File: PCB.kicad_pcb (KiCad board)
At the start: 4 copper layers, 33 parts, among them J2 JST - 1.00mm 4 Pin, SW1 MX_SW_solder, SW2 MX_SW_solder, SW3 MX_SW_solder, SW4 MX_SW_solder, SW72 SW_Push, SW73 SW_Push, U1 RP2040, U2 MX25R3235FZNxx0, U3 USBLC6-2SC6, U4 AP2127N3-1.2, Y1 Crystal_GND24_Small

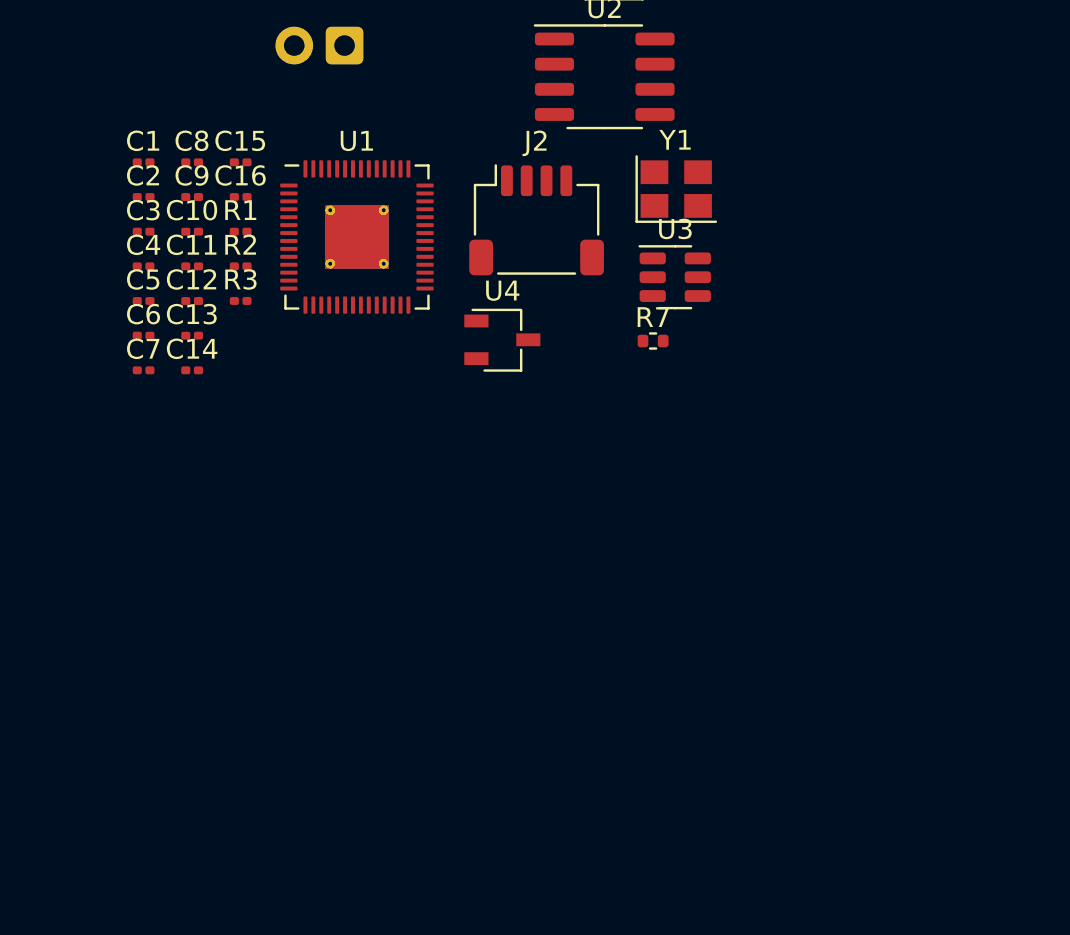
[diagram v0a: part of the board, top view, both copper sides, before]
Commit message: Updated LCSC part numbers for all parts.
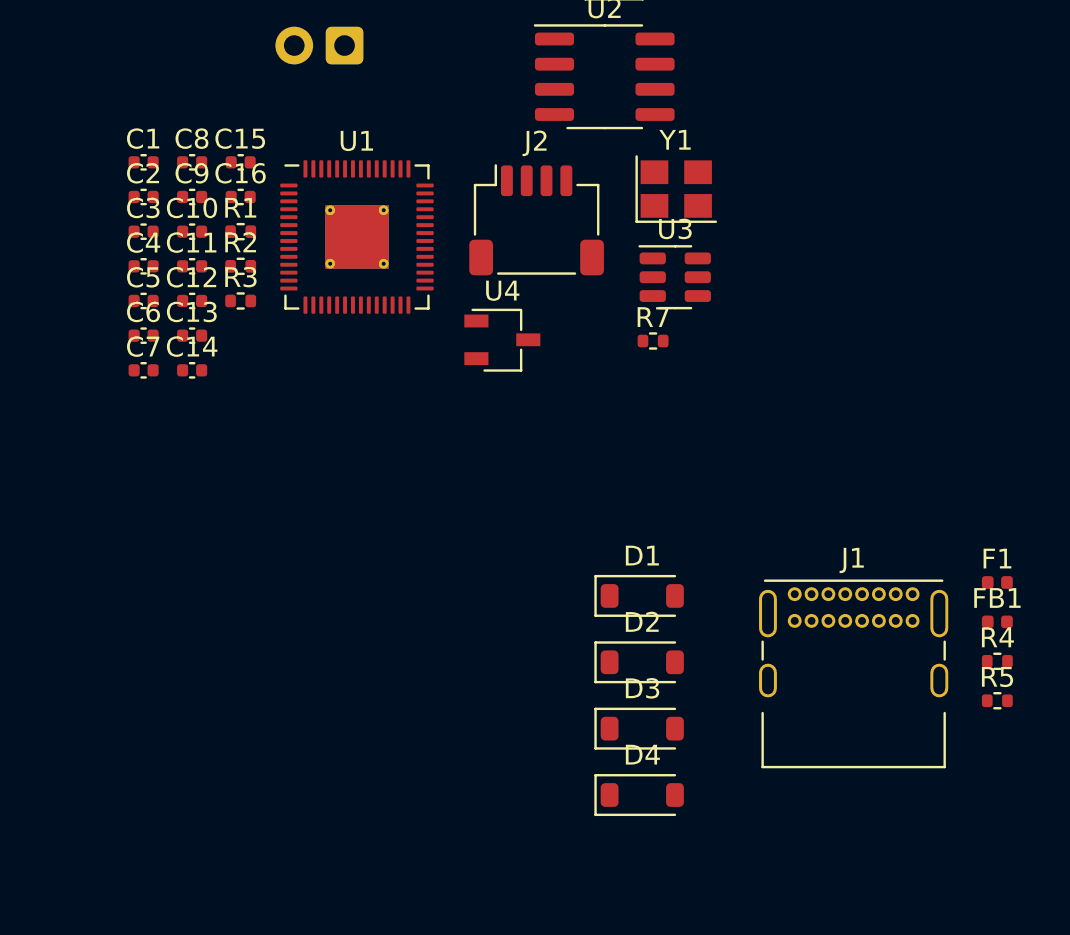
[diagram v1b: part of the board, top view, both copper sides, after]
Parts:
- added D1: D_Small, Diode_SMD:D_SOD-123, F.Cu at (82.6, 72.2)
- added D2: D_Small, Diode_SMD:D_SOD-123, F.Cu at (82.6, 75.6)
- added D3: D_Small, Diode_SMD:D_SOD-123, F.Cu at (82.6, 78.9)
- added D4: D_Small, Diode_SMD:D_SOD-123, F.Cu at (82.6, 82.3)
- added F1: 700mA, Fuse:Fuse_0402_1005Metric, F.Cu at (100.5, 71.5)
- added FB1: 100 Ohm @ 100 MHz, Inductor_SMD:L_0402_1005Metric, F.Cu at (100.5, 73.5)
- added J1: USB_C_Receptacle_USB2.0, Connector_USB:USB_C_Receptacle_GCT_USB4085, F.Cu at (90.3, 72.1)
- added R4: 5.1k, Resistor_SMD:R_0402_1005Metric, F.Cu at (100.5, 75.5)
- added R5: 5.1k, Resistor_SMD:R_0402_1005Metric, F.Cu at (100.5, 77.5)
- C1, C2: value 15p -> 30p; footprint Capacitor_SMD:C_0201_0603Metric -> Capacitor_SMD:C_0402_1005Metric
- C10, C11, C12, C13, C14, C15, C16, C3, C4, C5, C6, C7, C8, C9: footprint Capacitor_SMD:C_0201_0603Metric -> Capacitor_SMD:C_0402_1005Metric
- R1, R2, R3: footprint Resistor_SMD:R_0201_0603Metric -> Resistor_SMD:R_0402_1005Metric
- U2: value MX25R3235FZNxx0 -> SOP-8 SPI FLASH
- U4: value AP2127N3-1.2 -> 3.3V Fixed Regulator
- Y1: value Crystal_GND24_Small -> 12MHz Crystal 3225

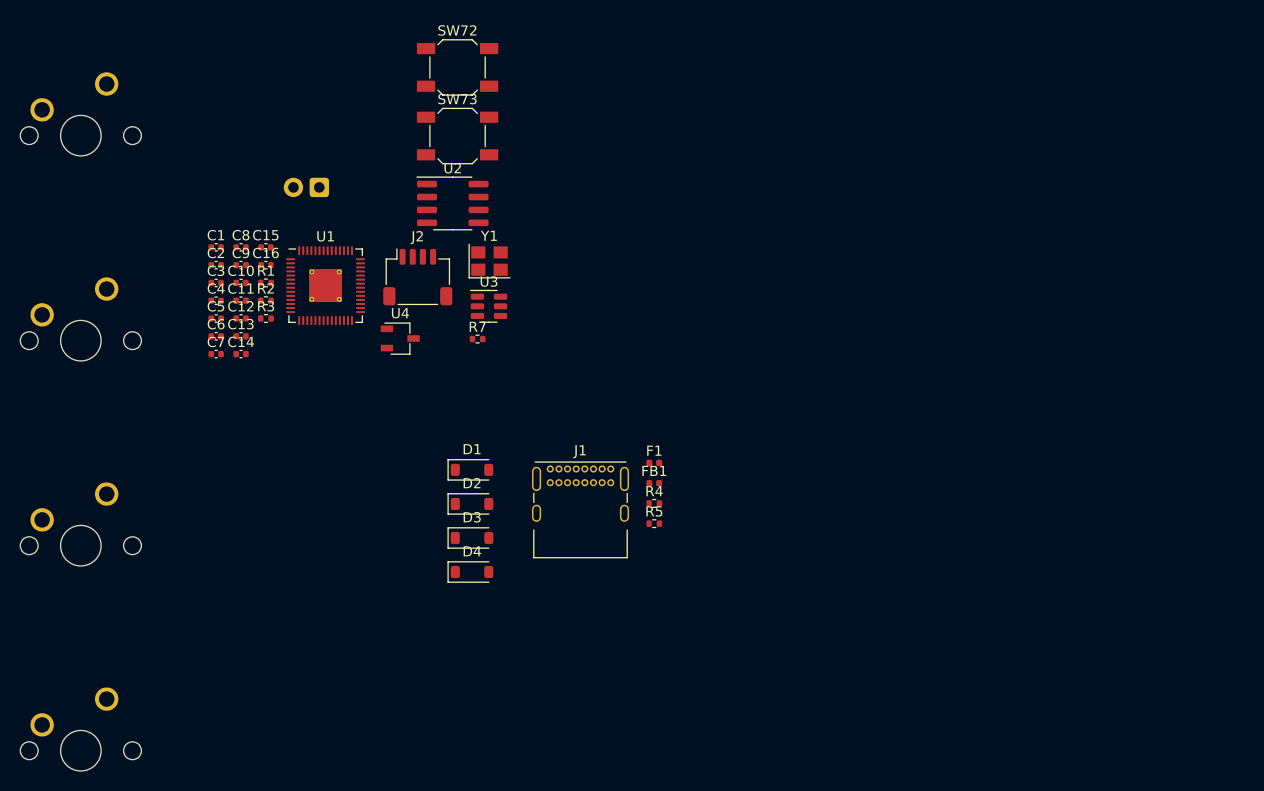
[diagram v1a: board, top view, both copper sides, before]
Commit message: Added missing decoupling capacitor and cr created example layout.
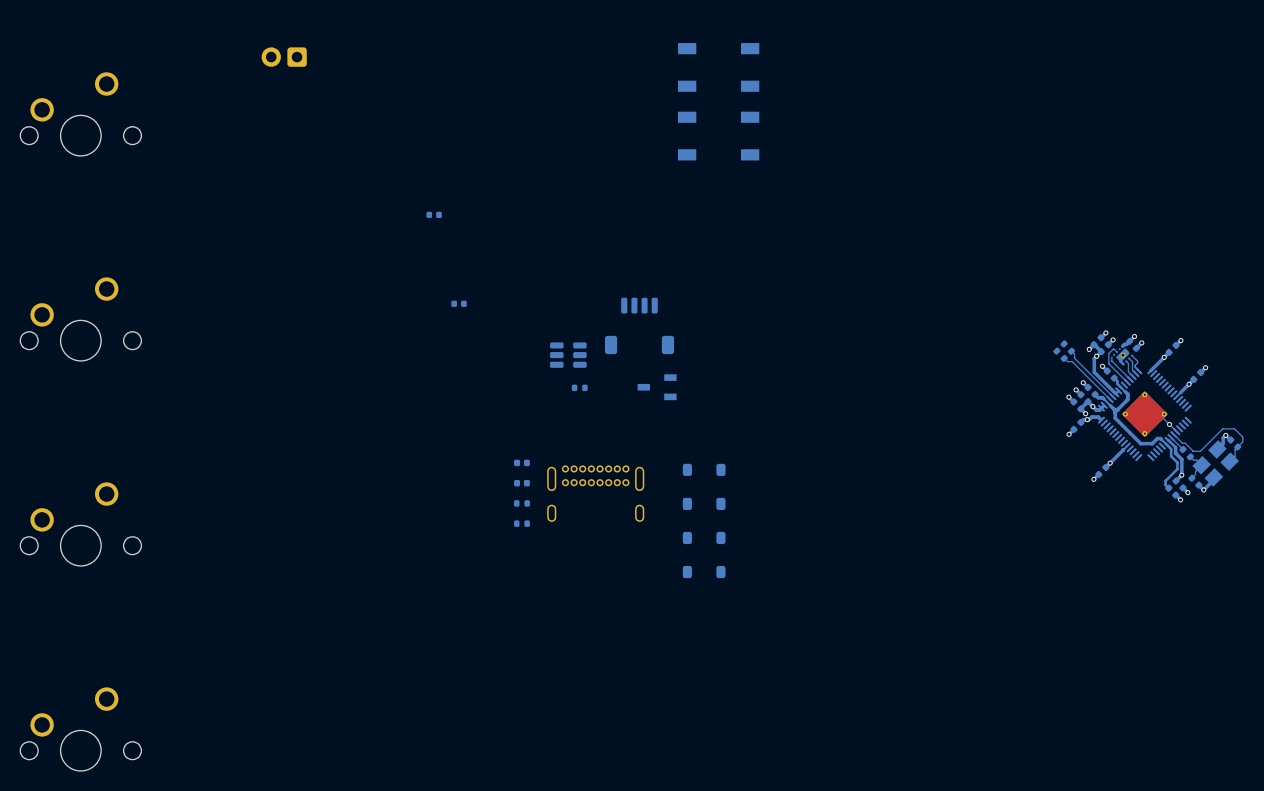
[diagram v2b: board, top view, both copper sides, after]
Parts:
- removed U2: SOP-8 SPI FLASH, Package_SO:SOP-8_3.76x4.96mm_P1.27mm
- added C17: 100n, Capacitor_SMD:C_0402_1005Metric, B.Cu at (151.5, 60.3)
- added U5: ZD25D40CNJGR, USON8:USON-8_1.5x1.5mm_P0.45mm, B.Cu at (146.6, 60.9)
- C1, C10, C11, C12, C13, C14, C15, C16, C2, C3, C4, C5, C6, C7, C8, C9, D1, D2, D3, D4, F1, FB1, J1, J2, R1, R2, R3, R4, R5, R7, SW72, SW73, U1, U3, U4, Y1: moved to B.Cu
- moved C1 102.0 mm to (157.6, 69.6), turned to 135 degrees
- moved C2 98.7 mm to (153.7, 73.4), turned to -45 degrees
- moved C9 94.7 mm to (153.9, 63.0), turned to 45 degrees
- moved C11 94.1 mm to (152.2, 73.6), turned to -45 degrees
- moved C16 91.9 mm to (151.4, 74.3), turned to -45 degrees
- moved R3 91.5 mm to (152.9, 70.6), turned to 135 degrees
- moved C10 88.0 mm to (147.6, 59.9), turned to -45 degrees
- moved C4 87.5 mm to (144.8, 60.2), turned to 45 degrees
- moved C8 87.5 mm to (144.6, 72.3), turned to -135 degrees
- moved C3 86.9 mm to (144.1, 59.5), turned to 45 degrees
- moved C6 85.6 mm to (142.8, 65.2), turned to 135 degrees
- moved C14 85.6 mm to (145.4, 62.8), turned to 135 degrees
- moved C5 85.2 mm to (142.1, 65.9), turned to 135 degrees
- moved C7 85.0 mm to (142.1, 67.9), turned to -135 degrees
- moved C12 84.0 mm to (143.5, 64.5), turned to 135 degrees
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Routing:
- net +3.3V: track 0.00 -> 26.6 mm, vias 0 -> 10
- net +1V1: track 0.00 -> 18.6 mm
- net GND: track 0.00 -> 18.6 mm, vias 0 -> 16
- net /XIN_: track 0.00 -> 11.7 mm
- net Net-(U1-USB_DM): track 0.00 -> 6.18 mm
- net Net-(U1-USB_DP): track 0.00 -> 6.17 mm
- net /SCLK_: track 0.00 -> 4.67 mm
- net /XOUT_: track 0.00 -> 3.12 mm
- net /SD0_: track 0.00 -> 2.95 mm
- net /CS_: track 0.00 -> 1.97 mm
- net /SD1_: track 0.00 -> 1.78 mm
- net /SD2_: track 0.00 -> 1.77 mm
- net Net-(U1-XOUT): track 0.00 -> 1.68 mm
